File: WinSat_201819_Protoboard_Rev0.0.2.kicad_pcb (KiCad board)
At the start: 4 copper layers, 41 x 62 mm, 61 parts, among them J1 Conn_01x02_Female, J2 Conn_01x02_Female, J3 Conn_01x02_Female, J4 Conn_01x02_Female, J5 Conn_01x03_Female, J6 Conn_01x02_Female, J7 JTAG-6PIN, J8 Conn_01x03_Female, P1 TPS82150, Q1 SSM3K329R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

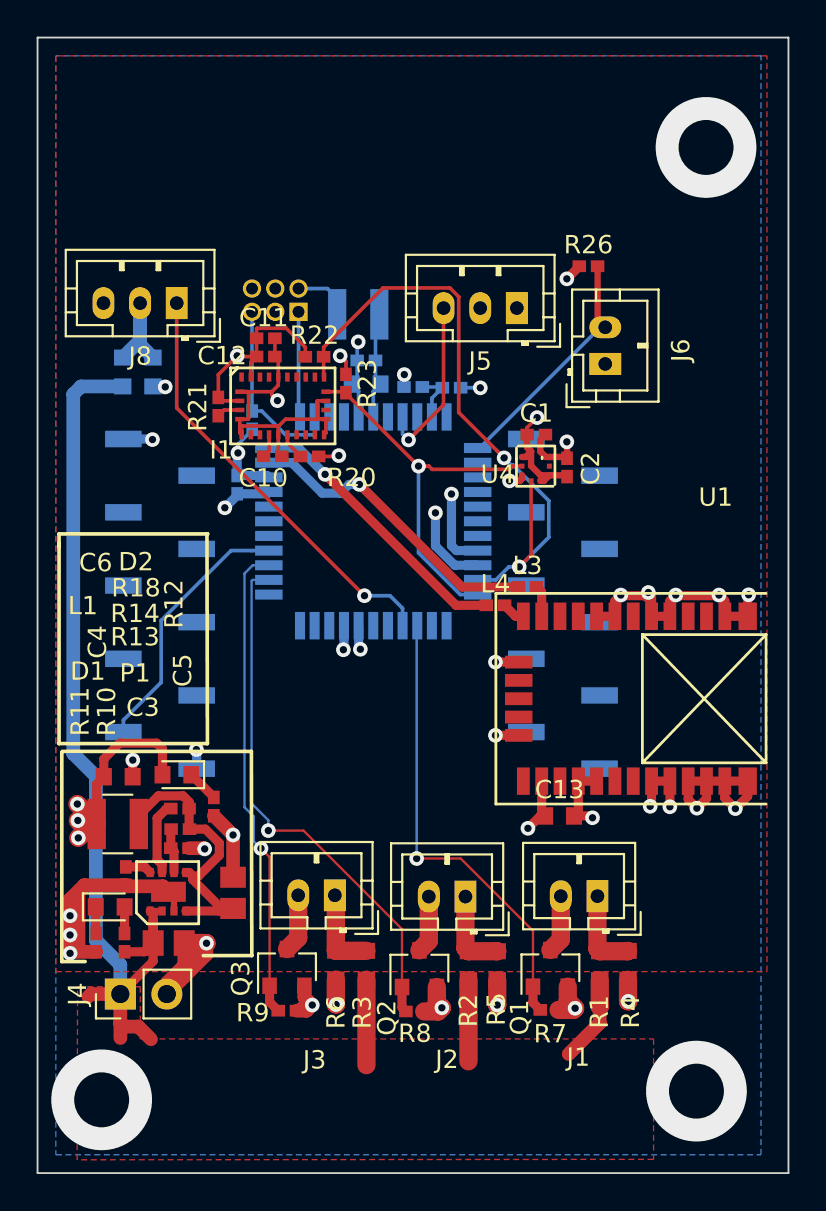
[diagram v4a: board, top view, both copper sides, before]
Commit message: V1.1.1 1M ESD
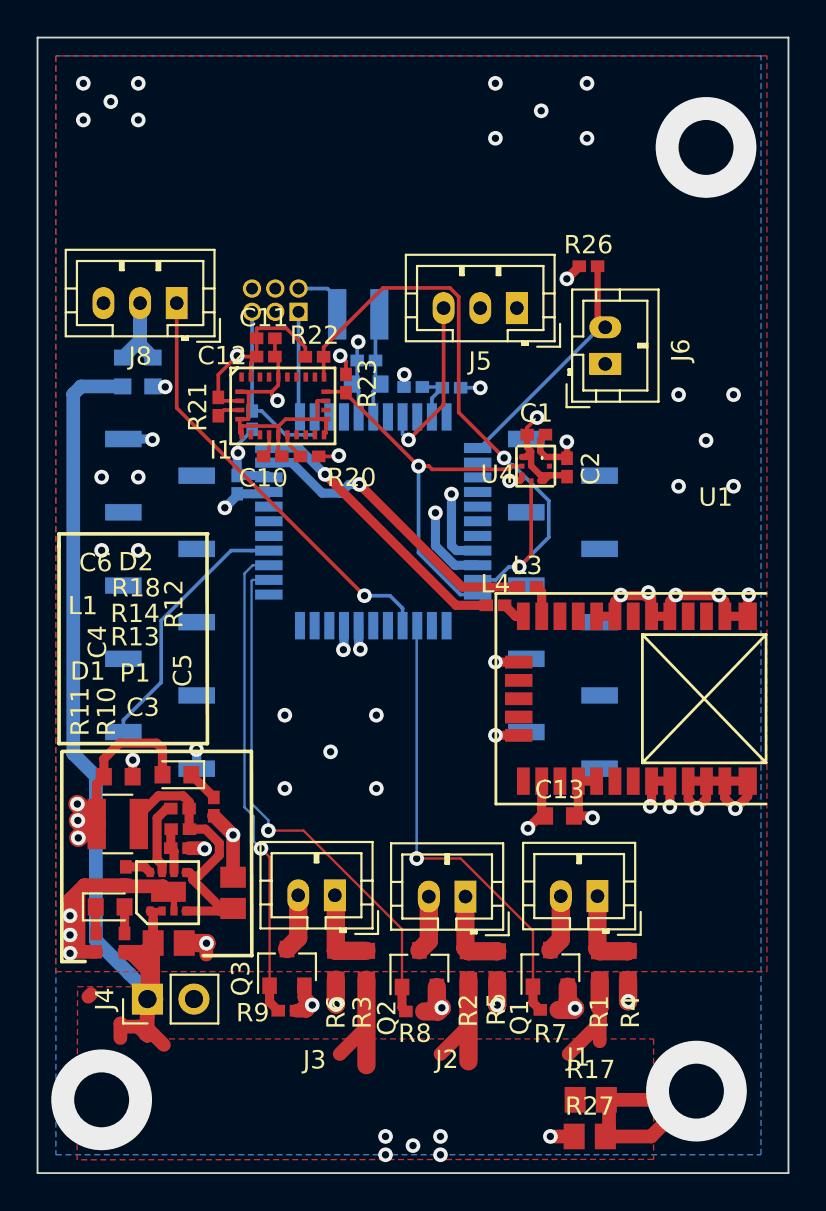
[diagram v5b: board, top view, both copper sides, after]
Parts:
- added R17: 1M, Resistor_SMD:R_0805_2012Metric, F.Cu at (94.2, 124.0)
- added R27: 1M, Resistor_SMD:R_0805_2012Metric, F.Cu at (94.2, 126.0)
- moved J4 1.51 mm to (70.0, 118.5)
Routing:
- net BAT_POS: track 65.8 -> 87.9 mm
- net +3V3: track 60.4 -> 70.0 mm, vias 19 -> 20
- net GND: track 117.5 -> 120.6 mm, vias 33 -> 62
